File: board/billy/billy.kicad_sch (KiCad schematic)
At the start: 73 parts, among them J1 Screw_Terminal_01x02, J10 Screw_Terminal_01x02, J11 Screw_Terminal_01x02, J2 Conn_01x06, J3 Screw_Terminal_01x02, J4 Screw_Terminal_01x02, J5 USB_B_Micro, J6 Screw_Terminal_01x02, J8 Screw_Terminal_01x03, J9 Screw_Terminal_01x02, Q1 AO3400A, Q2 AO3400A, Q3 AO3400A, Q4 AO3400A, SW1 TS-1088-AR02016, U1 ESP32-S3-WROOM-1, U2 DRV8833PWPR, U3 MAX98357A, U4 DRV8833PWPR, U8 USBLC6-2SC6

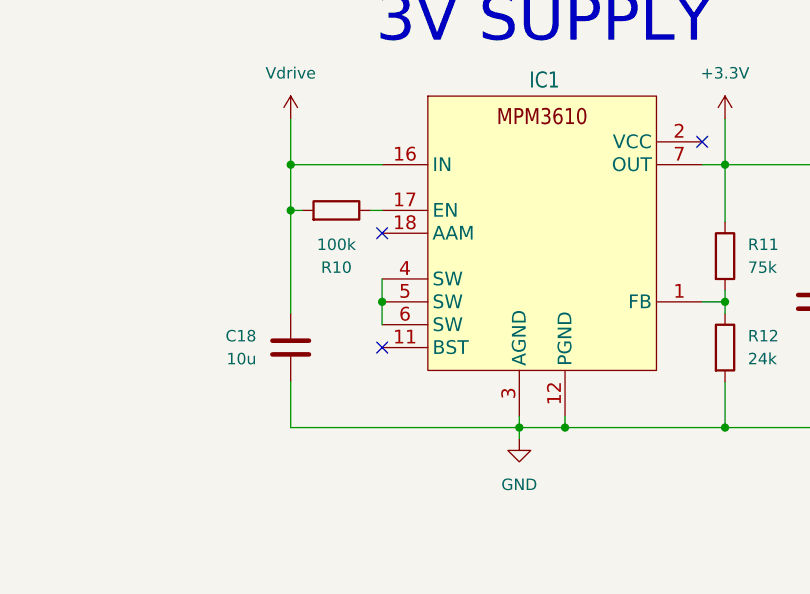
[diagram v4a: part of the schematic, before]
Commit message: Populate MPM3610 AAM resistor (R13, 82k) to enable light-load power-save mode
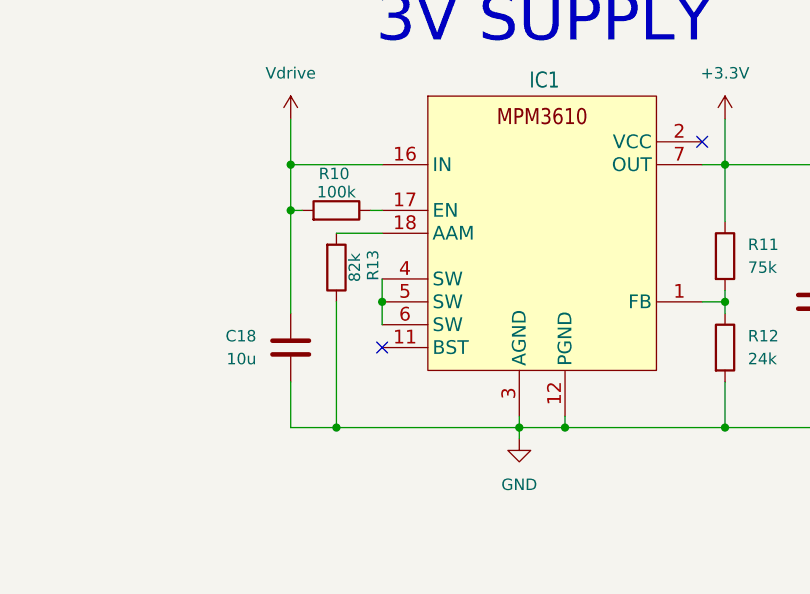
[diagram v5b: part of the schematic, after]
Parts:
- added R13: 82k, Resistor_SMD:R_0603_1608Metric, symbol Device:R
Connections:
- net GND: now also R13.1
- net at IC1.18 (AAM): now also R13.2
- no-connect marks 25 -> 24
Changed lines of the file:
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@@
 	)
 	(junction
+		(at 327.66 215.9)
+		(diameter 0)
+		(color 0 0 0 0)
+	)
+	(junction
 		(at 201.93 137.16)
 		(diameter 0)
@@
 	)
 	(no_connect
-		(at 332.74 194.31)
-	)
-	(no_connect
 		(at 142.24 107.95)
 	)
@@
 	(wire
 		(pts
+			(xy 327.66 194.31) (xy 332.74 194.31)
+		)
+		(stroke
+			(width 0)
+			(type default)
+		)
+	)
+	(wire
+		(pts
 			(xy 59.69 233.68) (xy 59.69 231.14)
 		)
@@
 	(wire
 		(pts
-			(xy 322.58 215.9) (xy 347.98 215.9)
+			(xy 322.58 215.9) (xy 327.66 215.9)
 		)
 		(stroke
@@
 	(wire
 		(pts
+			(xy 327.66 201.93) (xy 327.66 215.9)
+		)
+		(stroke
+			(width 0)
+			(type default)
+		)
+	)
+	(wire
+		(pts
 			(xy 370.84 210.82) (xy 370.84 215.9)
 		)
@@
 	(wire
 		(pts
+			(xy 327.66 215.9) (xy 347.98 215.9)
+		)
+		(stroke
+			(width 0)
+			(type default)
+		)
+	)
+	(wire
+		(pts
 			(xy 207.01 213.36) (xy 213.36 213.36)
 		)
@@
 	)
 	(symbol
+		(lib_id "Device:R")
+		(at 327.66 198.12 0)
+		(mirror x)
+		(unit 1)
+		(body_style 1)
+		(exclude_from_sim no)
+		(in_bom yes)
+		(on_board yes)
+		(in_pos_files yes)
+		(dnp no)
+		(property "Reference" "R13"
+			(at 331.724 197.866 90)
+			(show_name no)
+			(do_not_autoplace no)
+			(effects
+				(font
+					(size 1.27 1.27)
+				)
+			)
+		)
+		(property "Value" "82k"
+			(at 329.692 198.12 90)
+			(show_name no)
+			(do_not_autoplace no)
+			(effects
+				(font
+					(size 1.27 1.27)
+				)
+			)
+		)
+		(property "Footprint" "Resistor_SMD:R_0603_1608Metric"
+			(at 325.882 198.12 90)
+			(hide yes)
+			(show_name no)
+			(do_not_autoplace no)
+			(effects
+				(font
+					(size 1.27 1.27)
+				)
+			)
+		)
+		(property "Datasheet" ""
+			(at 327.66 198.12 0)
+			(hide yes)
+			(show_name no)
+			(do_not_autoplace no)
+			(effects
+				(font
+					(size 1.27 1.27)
+				)
+			)
+		)
+		(property "Description" "Resistor"
+			(at 327.66 198.12 0)
+			(hide yes)
+			(show_name no)
+			(do_not_autoplace no)
+			(effects
+				(font
+					(size 1.27 1.27)
+				)
+			)
+		)
+		(property "LCSC" "C23254"
+			(at 327.66 198.12 90)
+			(hide yes)
+			(show_name no)
+			(do_not_autoplace no)
+			(effects
+				(font
+					(size 1.27 1.27)
+				)
+			)
+		)
+		(pin "1"
+		)
+		(pin "2"
+		)
+		(instances
+			(project "billy"
+				(path "/bea121ec-f0fe-44e6-bdd2-ce74eb787ff8"
+					(reference "R13")
+					(unit 1)
+				)
+			)
+		)
+	)
+	(symbol
 		(lib_id "Device:C")
 		(at 71.12 210.82 0)
@@
 		(dnp no)
 		(property "Reference" "R10"
-			(at 327.66 198.12 90)
+			(at 327.406 187.706 90)
 			(show_name no)
 			(do_not_autoplace no)
@@
 		)
 		(property "Value" "100k"
-			(at 327.66 195.58 90)
+			(at 327.66 189.738 90)
 			(show_name no)
 			(do_not_autoplace no)

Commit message: Tighten board to JLCPCB fab limits and add BOOT/TTL header pins
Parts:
- added J5: Conn_01x02, Connector_PinHeader_2.54mm:PinHeader_1x02_P2.54mm_Vertical, symbol Connector_Generic:Conn_01x02
- added J6: Conn_01x03, Connector_PinHeader_2.54mm:PinHeader_1x03_P2.54mm_Vertical, symbol Connector_Generic:Conn_01x03
- added R1: 10k, Resistor_SMD:R_0603_1608Metric, symbol Device:R
- R2: renamed from R1; value 5.1k -> 10k; LCSC C23186 -> C25804
- renumbered C2 to C1, C16 to C15, C17 to C16, C18 to C17, C15 to C18, C21 to C19, C3 to C2, C19 to C20, C20 to C21, C1 to C3, C7 to C4, C4 to C5, C5 to C6, C6 to C7, J6 to J10, J8 to J11, J5 to J12, J9 to J7, J10 to J8, J11 to J9, R16 to R10, R8 to R11, R9 to R12, R10 to R13, R11 to R14, R13 to R15, R12 to R16, R18 to R17, R17 to R18, R2 to R3, R3 to R4, R4 to R5, R5 to R6, R6 to R7, R7 to R8, R15 to R9, IC1 to U6, U8 to U7, U6 to U8, U7 to U9
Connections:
- net +3.3V: now also R1.1
- net GND: now also J5.2 (Pin_2), J6.3 (Pin_3)
- net BOOT: now reaches U1.27 (GPIO0/BOOT)
- net BOOT: now also J5.1 (Pin_1), R1.2
- net U0RX: now reaches U1.36 (U0RXD/GPIO44/CLK_OUT2)
- net U0RX: now also J6.2 (Pin_2)
- net U0TX: now reaches U1.37 (U0TXD/GPIO43/CLK_OUT1)
- net U0TX: now also J6.1 (Pin_1)
- no-connect marks 24 -> 21
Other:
- note added: "BOOT"
- note added: "TTL"
- moved on the sheet: C1, C2, C3, J1, J2, J3, J4, R2, R3, R4, R5, SW1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

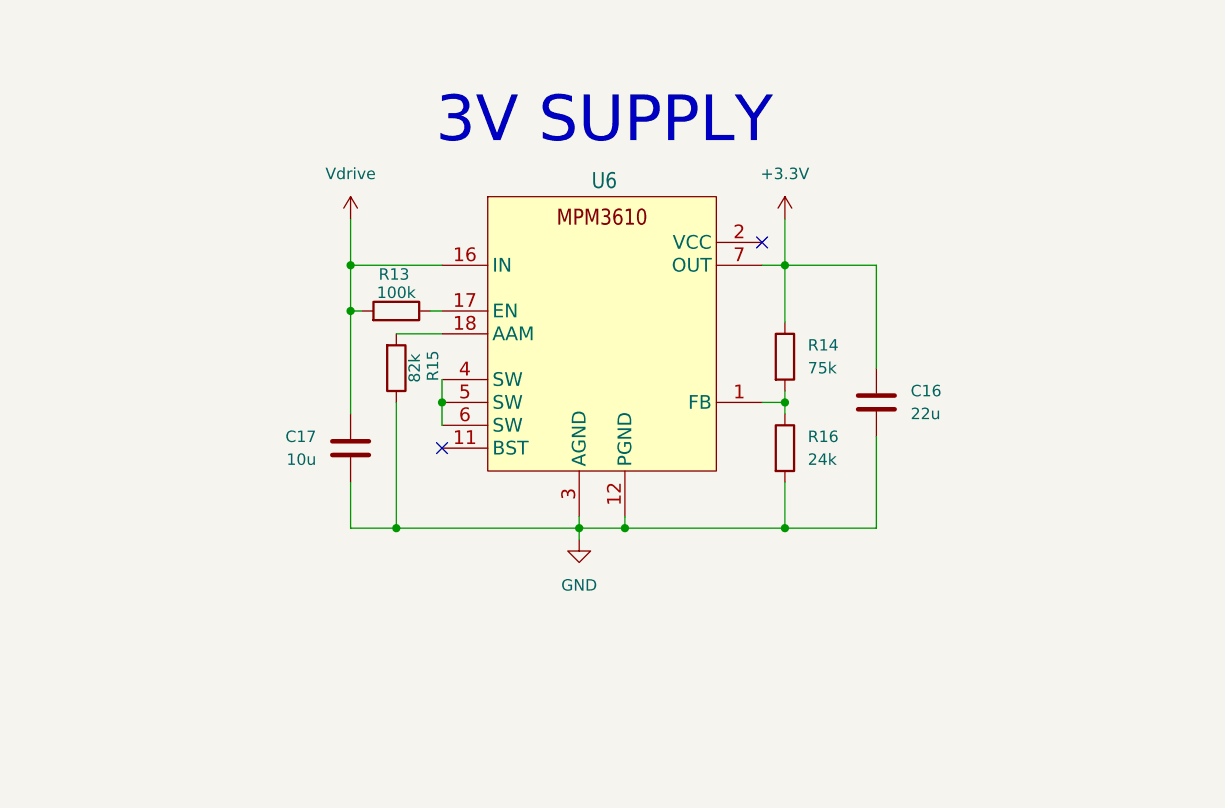
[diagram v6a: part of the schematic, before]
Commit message: Replace MPM3610 buck with Diodes AP63201, remove stale QFN-20 footprint
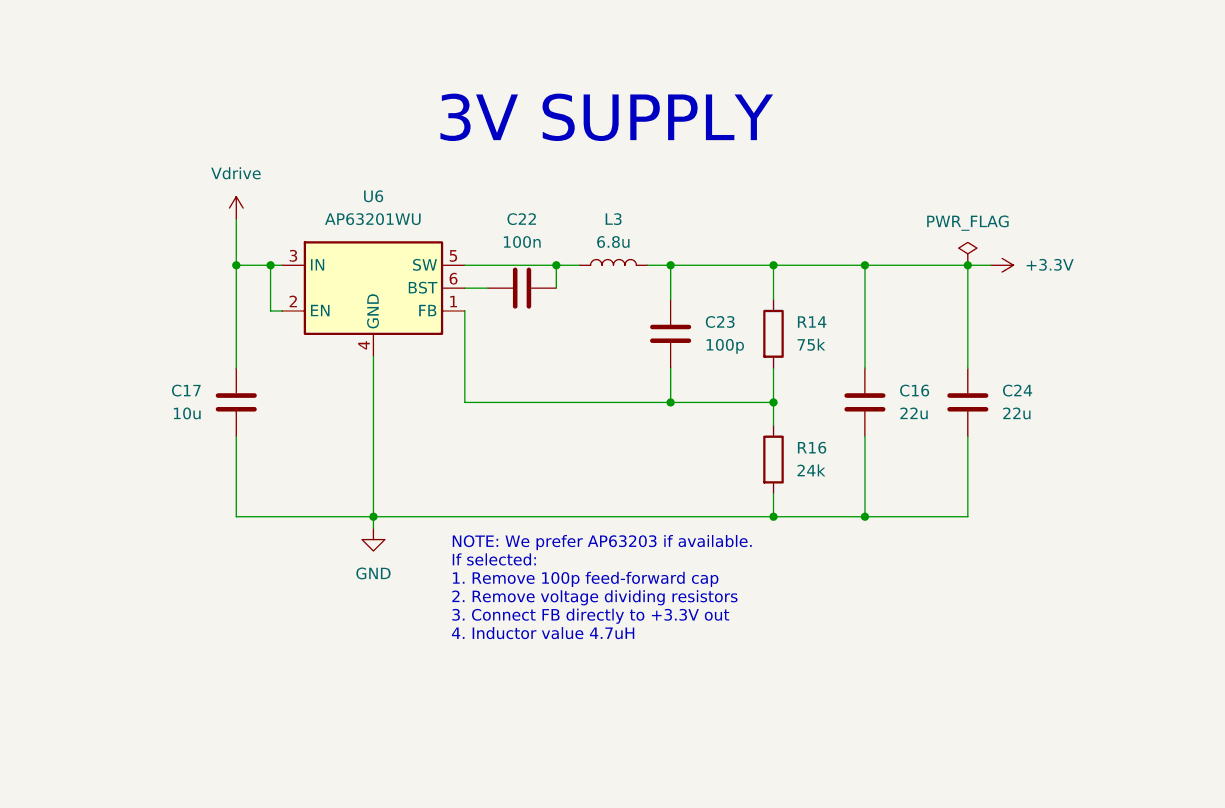
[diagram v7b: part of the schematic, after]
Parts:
- removed R13: 100k, Resistor_SMD:R_0603_1608Metric, symbol Device:R
- removed R15: 82k, Resistor_SMD:R_0603_1608Metric, symbol Device:R
- removed U6: (no value), billy:QFN-20, symbol billy:MPM3610
- added C22: 100n, Capacitor_SMD:C_0402_1005Metric, symbol Device:C
- added C23: 100p, Capacitor_SMD:C_0402_1005Metric, symbol Device:C
- added C24: 22u, Capacitor_SMD:C_0805_2012Metric, symbol Device:C
- added L3: 6.8u, Inductor_SMD:L_APV_ANR4030, symbol Device:L
- added U6: AP63201WU, Package_TO_SOT_SMD:TSOT-23-6, symbol Regulator_Switching:AP63201WU
- C17: footprint Capacitor_SMD:C_0805_2012Metric -> Capacitor_SMD:C_0603_1608Metric; LCSC C15850 -> C19702
- J2: LCSC C56816 -> C492414
- J5: LCSC (none) -> C492401
- J6: LCSC (none) -> C492411
- TP1, TP2, TP3: now left out of the parts list
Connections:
- net +3.3V: now also C23.1, C24.1, L3.2
- net GND: now also C24.2, U6.4 (GND)
- net Vdrive: now also U6.2 (EN), U6.3 (IN)
- net at R14.2, R16.1: now also C23.2, U6.1 (FB)
- new net: C22.2, L3.1, U6.5 (SW)
- new net: C22.1, U6.6 (BST)
- no-connect marks 21 -> 19
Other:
- note added: "NOTE: We prefer AP63203 if available. If selected: 1. Remove 100p feed-forward cap 2. Remove voltage dividing resistors 3. Connect FB directly to +3.3V out 4. Inductor value 4.7uH"
- moved on the sheet: C16, C17, R14, R16

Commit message: Consolidate decoupling caps to one 0603 10uF part across buck and rail bypass positions
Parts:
- C14, C7, C8: footprint Capacitor_SMD:C_0402_1005Metric -> Capacitor_SMD:C_0603_1608Metric; LCSC C15525 -> C19702
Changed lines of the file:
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@@
 			)
 		)
-		(property "Footprint" "Capacitor_SMD:C_0402_1005Metric"
+		(property "Footprint" "Capacitor_SMD:C_0603_1608Metric"
 			(at 257.5052 101.6 0)
 			(hide yes)
@@
 			)
 		)
-		(property "LCSC" "C15525"
+		(property "LCSC" "C19702"
 			(at 256.54 97.79 0)
 			(hide yes)
@@
 			)
 		)
-		(property "Footprint" "Capacitor_SMD:C_0402_1005Metric"
+		(property "Footprint" "Capacitor_SMD:C_0603_1608Metric"
 			(at 257.5052 148.59 0)
 			(hide yes)
@@
 			)
 		)
-		(property "LCSC" "C15525"
+		(property "LCSC" "C19702"
 			(at 256.54 144.78 0)
 			(hide yes)
@@
 			)
 		)
-		(property "Footprint" "Capacitor_SMD:C_0402_1005Metric"
+		(property "Footprint" "Capacitor_SMD:C_0603_1608Metric"
 			(at 331.1652 114.3 0)
 			(hide yes)
@@
 			)
 		)
-		(property "LCSC" "C15525"
+		(property "LCSC" "C19702"
 			(at 330.2 110.49 0)
 			(hide yes)
